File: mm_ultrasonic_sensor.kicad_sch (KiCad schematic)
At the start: 0 parts

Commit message: tp2
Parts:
- added C7: 2.2uF 16V, symbol Device:C_Small
- added C7: 0.1uF 16V, symbol Device:C_Small
- added R8: 100, Resistor_SMD:R_0603_1608Metric, symbol Device:R
- added U4: HC-SR04, minimouse:HC-SR04, symbol minimouse:HC-SR04
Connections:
- net SONAR_ECHO: now also R8.1
- net SONAR_TRIGGER: now also U4.2 (TRIG)
- new net: R8.2, U4.3 (ECHO)
- new net +BATT: C7.1, C7.1, U4.4 (VCC)
- new net GND: C7.2, C7.2, U4.1 (GND)

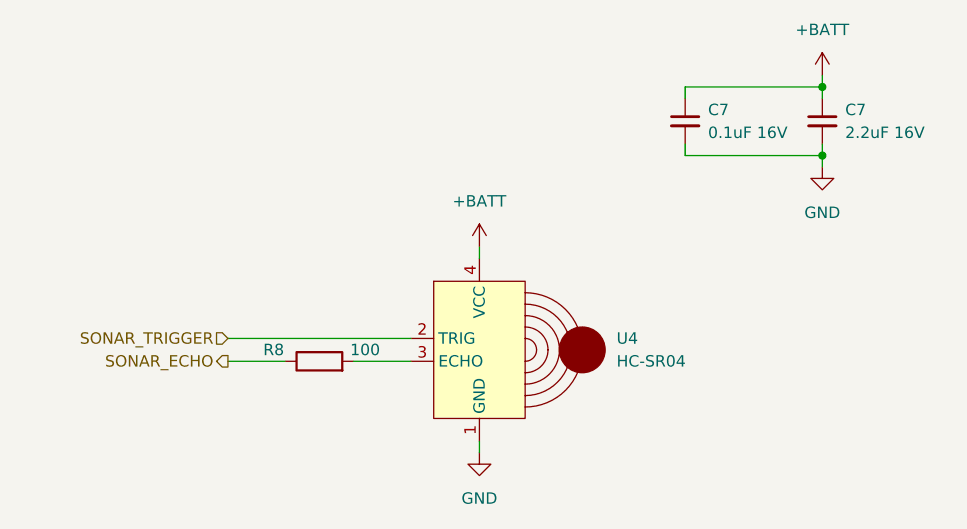
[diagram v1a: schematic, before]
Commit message: updated to kicad 8.0
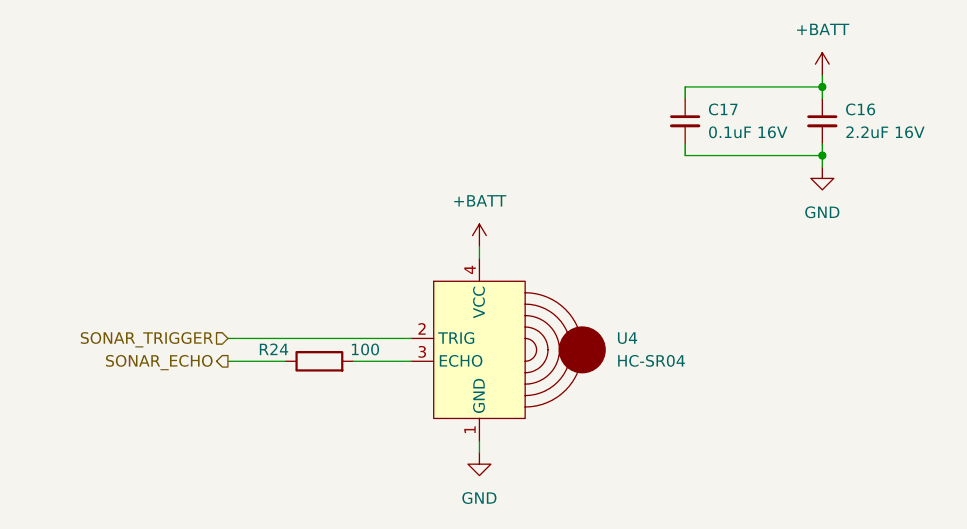
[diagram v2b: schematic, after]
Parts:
- renumbered C7 to C16, C7 to C17, R8 to R24
